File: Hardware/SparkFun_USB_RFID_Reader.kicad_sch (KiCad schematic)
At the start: 29 parts, among them J1 USB_C_Receptacle, J2 Conn_01x07_2.0mm, J3 Conn_01x05_2.0mm, J5 Conn_01x08, Q1 MMBT2222A, U3 CH340C

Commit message: Rename files
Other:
- note added: "External Header"
- note added: "RFID Module Connector"
- note removed: "0.1" Header"
- note removed: "RFID Module Header"
- title: USB-C RFID Breakout -> SparkFun USB RFID Reader
- moved on the sheet: BZ1, C1, C2, C3, C4, D1, J1, J2, J3, O1, Q1, R1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

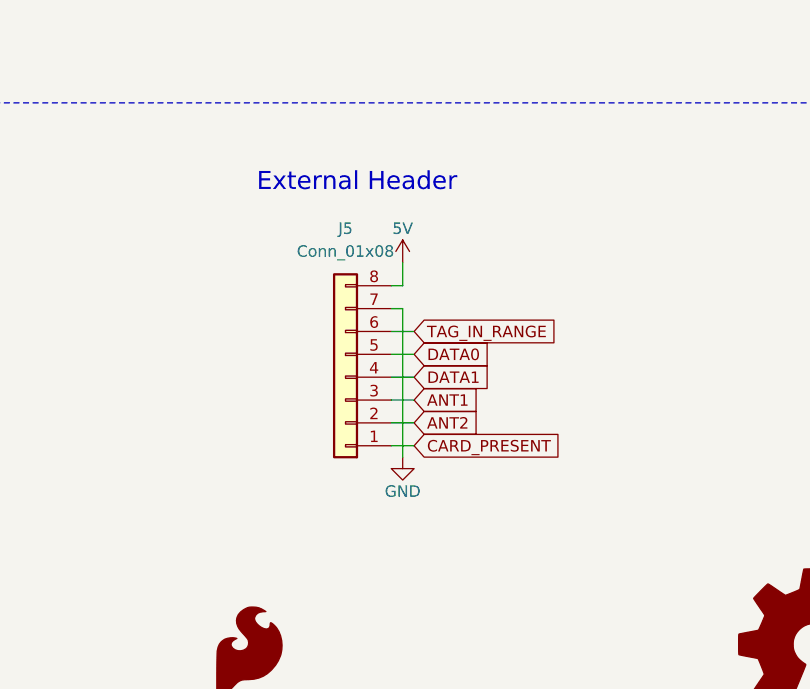
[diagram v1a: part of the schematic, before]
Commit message: Center USB-C Connector
- Move USB-C connector to center
- Arrange 0.1" headers to either side
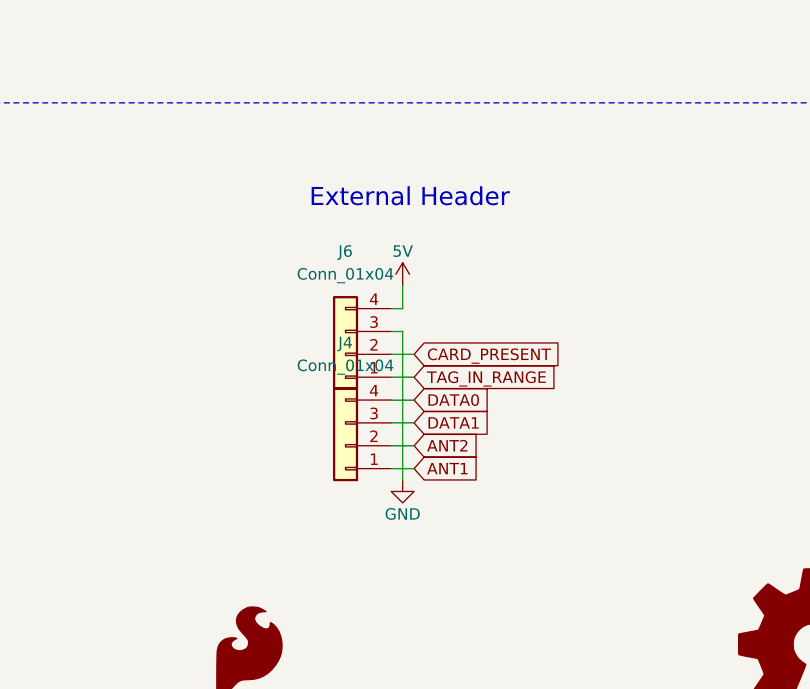
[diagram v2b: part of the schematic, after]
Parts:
- removed J5: Conn_01x08, SparkFun-Connector:1x08, symbol SparkFun-Connector:Conn_01x08
- added J4, J6: Conn_01x04, SparkFun-Connector:1x04, symbol SparkFun-Connector:Conn_01x04
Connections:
- net 5V: now also J6.4 (Pin_4)
- net ANT1: now also J4.1 (Pin_1)
- net ANT2: now also J4.2 (Pin_2)
- net CARD_PRESENT: now also J6.2 (Pin_2)
- net DATA0: now also J4.4 (Pin_4)
- net DATA1: now also J4.3 (Pin_3)
- net GND: now also J6.3 (Pin_3)
- net TAG_IN_RANGE: now also J6.1 (Pin_1)

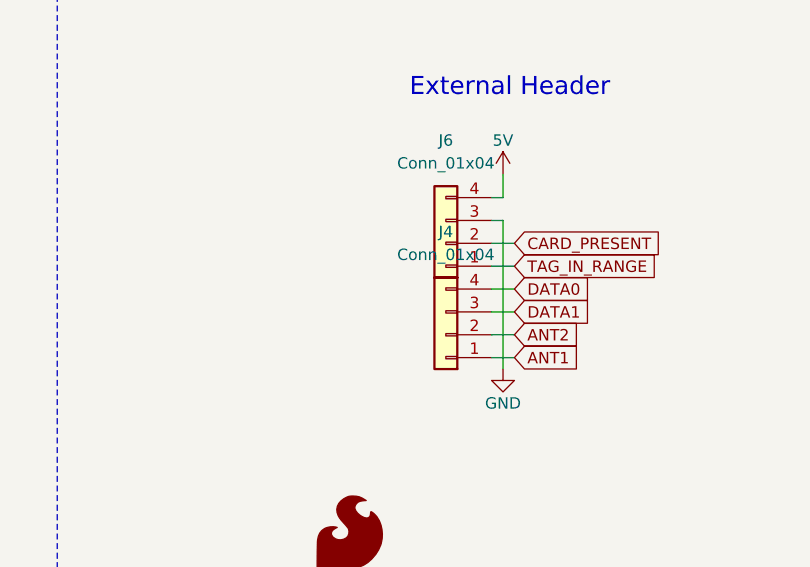
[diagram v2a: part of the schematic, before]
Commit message: Move fiducial from silk. Add version in copper. Move OSHW gear from silk.
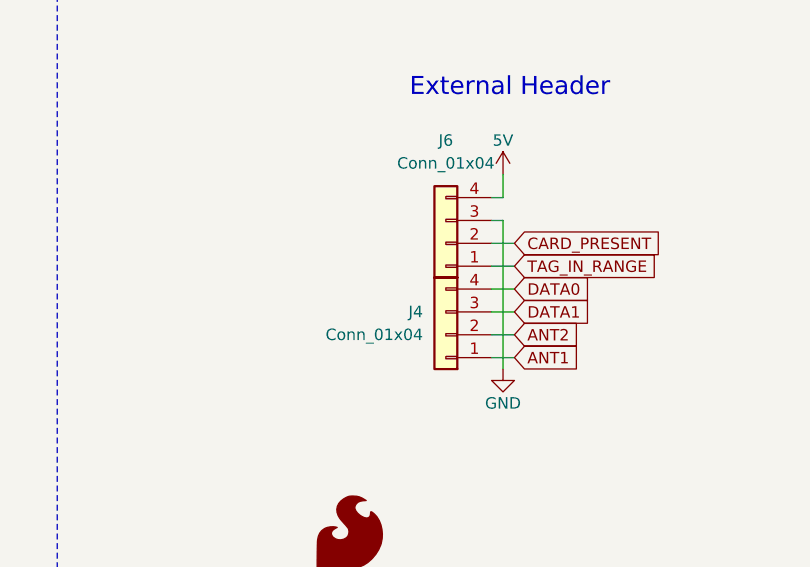
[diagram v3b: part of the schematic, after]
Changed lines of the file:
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@@
 		(fields_autoplaced yes)
 		(property "Reference" "J4"
-			(at 203.2 123.19 0)
+			(at 200.66 132.0799 0)
 			(effects
 				(font
 					(size 1.27 1.27)
 				)
+				(justify left)
 			)
 		)
 		(property "Value" "Conn_01x04"
-			(at 203.2 125.73 0)
+			(at 200.66 134.6199 0)
 			(effects
 				(font
 					(size 1.27 1.27)
 				)
+				(justify left)
 			)
 		)

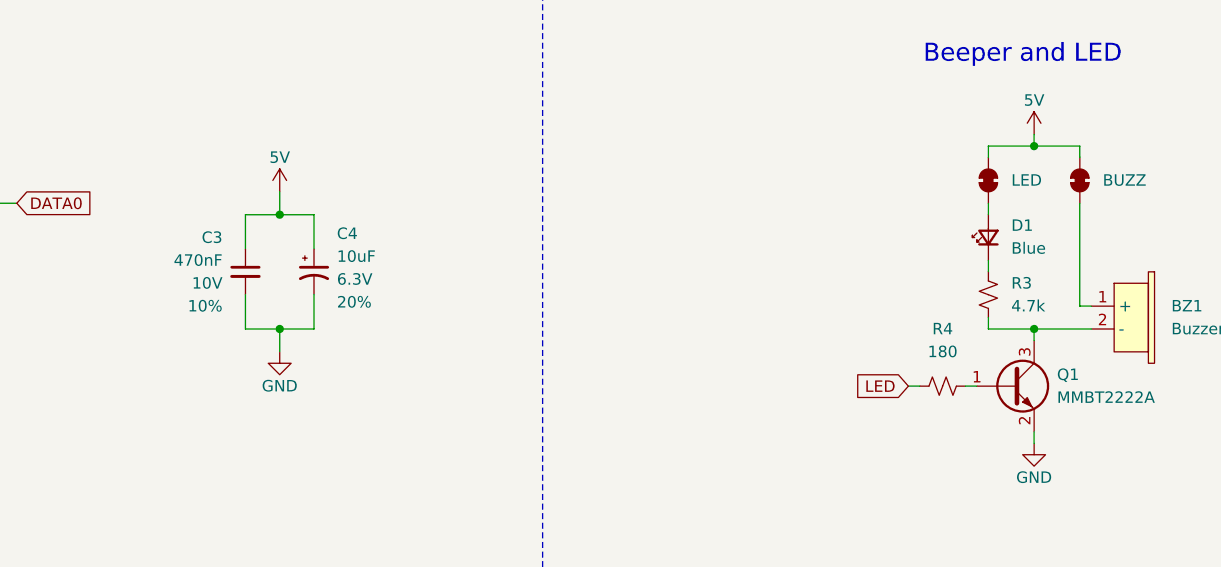
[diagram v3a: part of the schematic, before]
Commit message: Change decoupling cap. Change LED resistor.
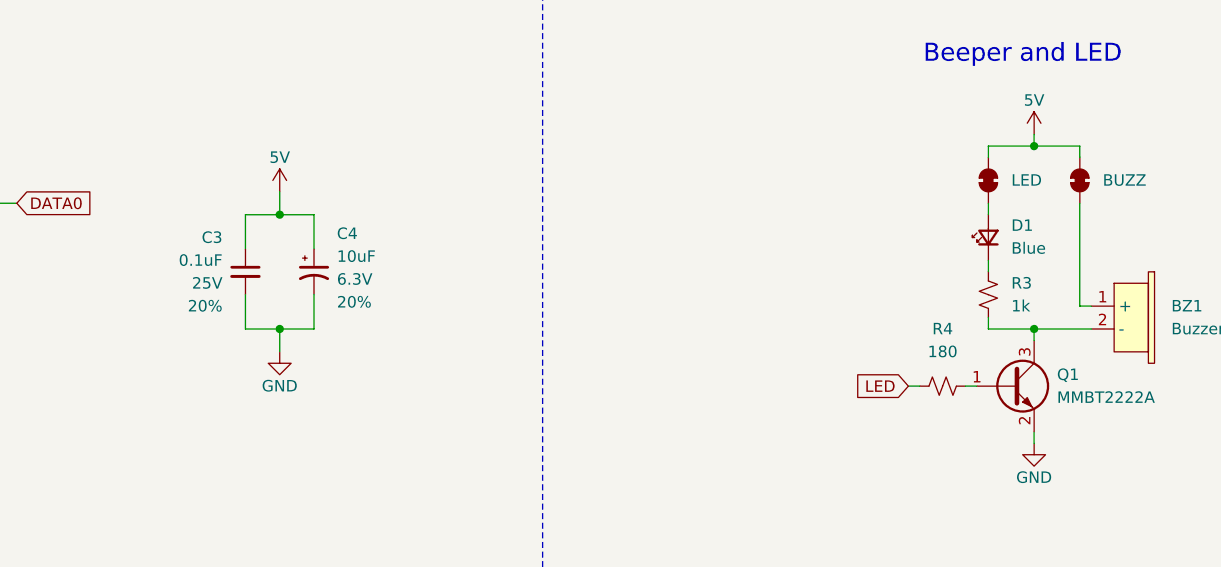
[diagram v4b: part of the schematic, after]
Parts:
- C3: value 470nF -> 0.1uF; symbol SparkFun-Capacitor:470nF_0603_10V_10% -> SparkFun-Capacitor:0.1uF_0603_25V_20%; PROD_ID CAP-13216 -> CAP-00810; Tolerance 10% -> 20%; Voltage 10V -> 25V
- R3: value 4.7k -> 1k; symbol SparkFun-Resistor:4.7k_0603 -> SparkFun-Resistor:1k_0603; PROD_ID RES-07857 -> RES-07856
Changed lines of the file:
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@@
 	)
 	(symbol
-		(lib_id "SparkFun-Resistor:4.7k_0603")
+		(lib_id "SparkFun-Resistor:1k_0603")
 		(at 209.55 60.96 90)
 		(unit 1)
@@
 			)
 		)
-		(property "Value" "4.7k"
+		(property "Value" "1k"
 			(at 212.09 62.2299 90)
 			(effects
@@
 		)
 		(property "Footprint" "SparkFun-Resistor:R_0603_1608Metric"
-			(at 213.868 60.96 0)
+			(at 214.122 60.96 0)
 			(effects
 				(font
@@
 		)
 		(property "Datasheet" "https://www.vishay.com/docs/20035/dcrcwe3.pdf"
-			(at 218.44 60.96 0)
+			(at 218.44 62.23 0)
 			(effects
 				(font
@@
 			)
 		)
-		(property "PROD_ID" "RES-07857"
-			(at 216.154 60.96 0)
+		(property "PROD_ID" "RES-07856"
+			(at 216.408 60.96 0)
 			(effects
 				(font
@@
 	)
 	(symbol
-		(lib_id "SparkFun-Capacitor:470nF_0603_10V_10%")
+		(lib_id "SparkFun-Capacitor:0.1uF_0603_25V_20%")
 		(at 127 58.42 0)
 		(unit 1)
@@
 			)
 		)
-		(property "Value" "470nF"
+		(property "Value" "0.1uF"
 			(at 124.46 57.1562 0)
 			(effects
@@
 		)
 		(property "Datasheet" "https://cdn.sparkfun.com/assets/8/a/4/a/5/Kemet_Capacitor_Datasheet.pdf"
-			(at 127 74.93 0)
+			(at 127 72.39 0)
 			(effects
 				(font
@@
 			)
 		)
-		(property "PROD_ID" "CAP-13216"
-			(at 127 72.39 0)
-			(effects
-				(font
-					(size 1.27 1.27)
-				)
-				(hide yes)
-			)
-		)
-		(property "Voltage" "10V"
+		(property "PROD_ID" "CAP-00810"
+			(at 127 74.93 0)
+			(effects
+				(font
+					(size 1.27 1.27)
+				)
+				(hide yes)
+			)
+		)
+		(property "Voltage" "25V"
 			(at 124.46 59.6962 0)
 			(effects
@@
 			)
 		)
-		(property "Tolerance" "10%"
+		(property "Tolerance" "20%"
 			(at 124.46 62.2362 0)
 			(effects

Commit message: Change to PTH connectors
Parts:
- J2: footprint SparkFun-Connector:1x07_2.0mm_SMD_Pin1RightDown -> SparkFun-Connector:1x07_2.0mm; symbol SparkFun-Connector:Conn_01x07_2.0mm_SMD_Pin1RightDown -> SparkFun-Connector:Conn_01x07_2.0mm; PROD_ID CONN-09345 -> CONN-09001
- J3: footprint SparkFun-Connector:1x05_2.0mm_SMD_Pin1RightDown -> SparkFun-Connector:1x05_2.0mm; symbol SparkFun-Connector:Conn_01x05_2.0mm_SMD_Pin1RightDown -> SparkFun-Connector:Conn_01x05_2.0mm; PROD_ID CONN-09344 -> CONN-09000
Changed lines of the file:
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@@
 	)
 	(symbol
-		(lib_id "SparkFun-Connector:Conn_01x05_2.0mm_SMD_Pin1RightDown")
+		(lib_id "SparkFun-Connector:Conn_01x05_2.0mm")
 		(at 53.34 151.13 0)
 		(mirror x)
@@
 			)
 		)
-		(property "Footprint" "SparkFun-Connector:1x05_2.0mm_SMD_Pin1RightDown"
+		(property "Footprint" "SparkFun-Connector:1x05_2.0mm"
 			(at 53.34 140.97 0)
 			(effects
@@
 			)
 		)
-		(property "Datasheet" "https://drawings-pdf.s3.amazonaws.com/10489.pdf"
+		(property "Datasheet" "https://www.mouser.com/datasheet/2/837/bf085-1994323.pdf"
 			(at 53.34 138.43 0)
 			(effects
@@
 			)
 		)
-		(property "Description" "5 pos 2mm pitch 4.4mm tall female SMD header."
+		(property "Description" "5 pos 2mm pitch 4.4mm tall female header."
 			(at 53.34 135.89 0)
 			(effects
@@
 			)
 		)
-		(property "PROD_ID" "CONN-09344"
+		(property "PROD_ID" "CONN-09000"
 			(at 53.34 133.35 0)
 			(effects
@@
 	)
 	(symbol
-		(lib_id "SparkFun-Connector:Conn_01x07_2.0mm_SMD_Pin1RightDown")
+		(lib_id "SparkFun-Connector:Conn_01x07_2.0mm")
 		(at 102.87 148.59 0)
 		(mirror y)
@@
 			)
 		)
-		(property "Footprint" "SparkFun-Connector:1x07_2.0mm_SMD_Pin1RightDown"
+		(property "Footprint" "SparkFun-Connector:1x07_2.0mm"
 			(at 102.87 163.83 0)
 			(effects
@@
 			)
 		)
-		(property "Datasheet" "https://drawings-pdf.s3.amazonaws.com/10489.pdf"
+		(property "Datasheet" "https://www.mouser.com/datasheet/2/837/bf085-1994323.pdf"
 			(at 102.87 166.37 0)
 			(effects
@@
 			)
 		)
-		(property "Description" "7 pos 2mm pitch 4.4mm tall female SMD header."
+		(property "Description" "7 pos 2mm pitch 4.4mm tall female"
 			(at 102.87 168.91 0)
 			(effects
@@
 			)
 		)
-		(property "PROD_ID" "CONN-09345"
+		(property "PROD_ID" "CONN-09001"
 			(at 102.87 161.29 0)
 			(effects

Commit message: Post design review fixes
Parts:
- removed FID2, FID3: Fiducial_0.5mm, SparkFun-Aesthetic:Fiducial_0.5mm_Mask1mm, symbol SparkFun-Aesthetic:Fiducial_0.5mm
- added D2: DT1042-04SO, SparkFun-Semiconductor-Standard:SOT23-6, symbol SparkFun-DiscreteSemi:D_TVS_ESD_USB
- added F1: 6V/0.5A/1A, SparkFun-Fuse:0805, symbol SparkFun-Fuse:Fuse 6V/0.5A/1A
- added J5, J7: Conn_01x01, SparkFun-Connector:1x01, symbol SparkFun-Connector:Conn_01x01
- added JP3: SHLD, SparkFun-Jumper:Jumper_2_NC_Trace, symbol SparkFun-Jumper:SolderJumper_2_Bridged
- added JP5: MD1, SparkFun-Jumper:Jumper_2_NO, symbol SparkFun-Jumper:SolderJumper_2_Open
- added JP7: MD2, SparkFun-Jumper:Jumper_2_NO, symbol SparkFun-Jumper:SolderJumper_2_Open
- added R5, R6, R7, R8, R9: 4.7k, SparkFun-Resistor:R_0603_1608Metric, symbol SparkFun-Resistor:4.7k_0603
- C4: footprint SparkFun-Capacitor:C_0603_1608Metric_Polar -> SparkFun-Capacitor:C_0603_1608Metric; symbol SparkFun-Capacitor:10uF_0603_6.3V_20%_Polar(Tant) -> SparkFun-Capacitor:10uF_0603_10V_20%; PROD_ID CAP-13210 -> CAP-20155; Voltage 6.3V -> 10V
- D1: value Blue -> Green; footprint SparkFun-LED:LED_0603_1608Metric_Blue -> SparkFun-LED:LED_0603_1608Metric_Green; symbol SparkFun-LED:LED_Blue_0603 -> SparkFun-LED:LED_Green_0603; PROD_ID DIO-08575 -> DIO-00821
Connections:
- net CARD_PRESENT: now also R9.1
- net DATA0: now also R7.1
- net DATA1: now also J2.3 (Pin_3), R8.1; no longer J2.5 (Pin_5)
- net GND: now also D2.2 (GND), JP3.1 (A), R6.1; no longer J2.6 (Pin_6)
- net LED: now also J2.5 (Pin_5), JP7.2 (B); no longer J2.3 (Pin_3)
- net TAG_IN_RANGE: now also J2.1 (Pin_1); no longer J2.7 (Pin_7)
- net FORMAT: now reaches J2.2 (Pin_2)
- net FORMAT: now also JP5.1 (A), JP7.1 (A), R6.2
- net at J1.A6 (D+), J1.B6 (D+), U3.5 (UD+): now also D2.3 (I/O2)
- net at J1.A7 (D-), J1.B7 (D-), U3.6 (UD-): now also D2.6 (I/O4)
- net at J1.S (SHIELD): now also JP3.2 (B)
- net at U3.2 (TXD): now also J5.1 (Pin_1)
- net 5V renamed VUSB
- net VUSB: now also J2.7 (Pin_7), F1.2, JP5.2 (B), R5.2, R7.2, R8.2, R9.2; no longer J1.VBUS, J2.1 (Pin_1), J3.2 (Pin_2)
- new net: F1.1, J1.VBUS
- new net ~{RST}: J3.2 (Pin_2), J7.1 (Pin_1), R5.1
- no-connect marks 0 -> 11
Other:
- note added: "ASCII"
- note added: "Closed"
- note added: "Format"
- note added: "MD1"
- note added: "MD2"
- note added: "Magnet"
- note added: "Open"
- note added: "Output Format Select"
- note added: "Wiegand"
- company: (none) -> SparkFun
- moved on the sheet: C1, C2, C3, J3, O1, U3
